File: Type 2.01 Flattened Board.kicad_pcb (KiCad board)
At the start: 4 copper layers, 170 x 170 mm, 74 parts, among them J1 Conn_02x28_Odd_Even, J10 Conn_01x02, J2 Conn_02x18_Odd_Even, J3 Conn_01x01, J4 Conn_02x03_Odd_Even, J5 Conn_02x03_Odd_Even, J6 Conn_02x28_Odd_Even, J7 Conn_01x08, J8 Conn_01x01, J9 Conn_01x01, U1 74LVC1G79, U11 74AHC245, U13 74AHC04, U14 ATmega4809-PF, U16 ATmega4809-PF, U17 74AHC157, U18 74AHC573, U19 74AHC573, U2 74AHC245, U20 Adafruit_FeatherWing, U21 Adafruit_FeatherWing, U3 74AHC138, U4 74AHC245, U5 74AHC245, U6 74AHC245, U7 74LVC8T245, U8 74LVC8T245, U9 i960Sx_PLCC84

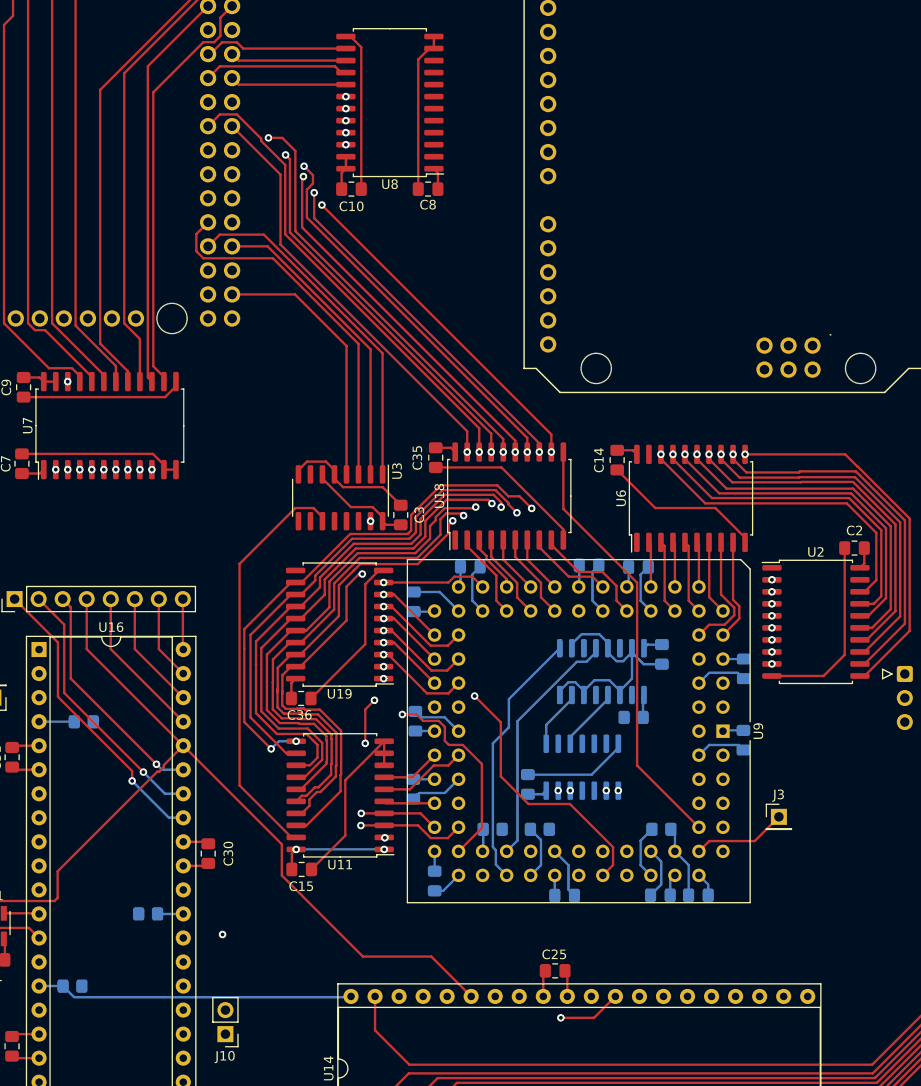
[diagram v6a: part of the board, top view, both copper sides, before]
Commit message: More traces laid out
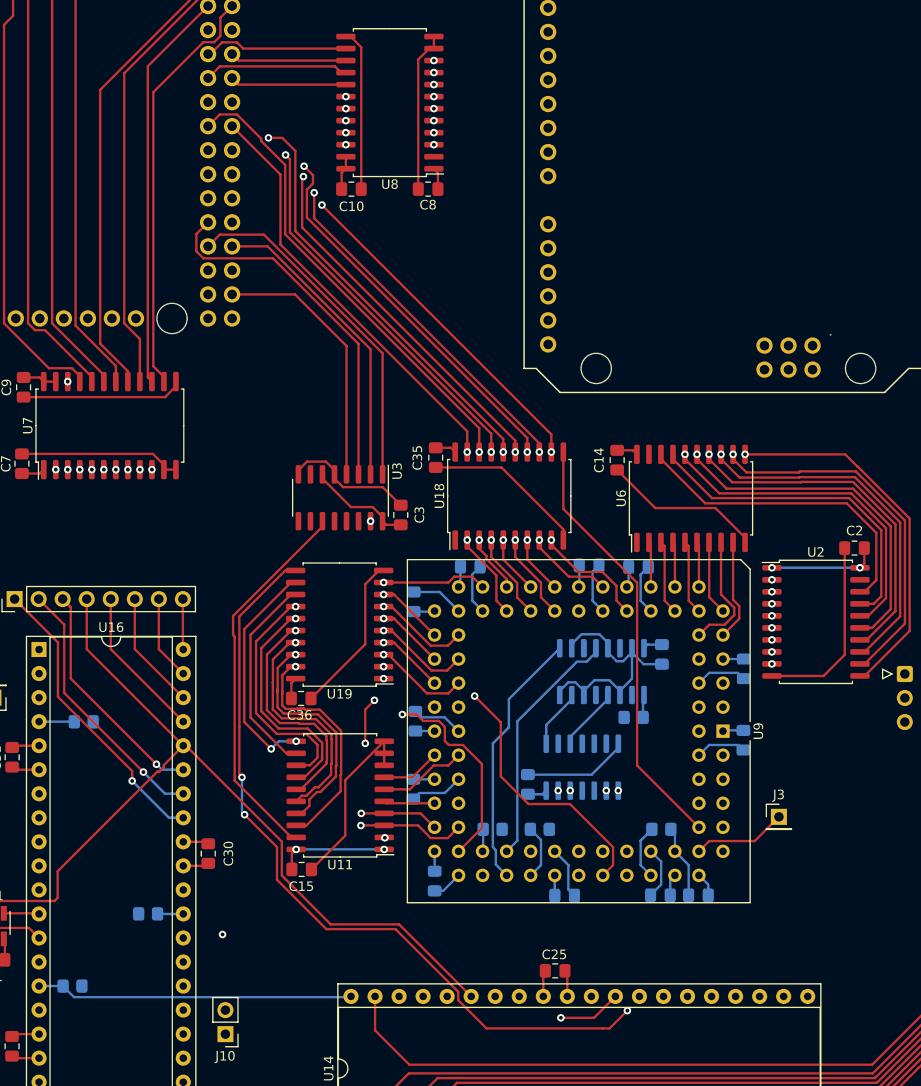
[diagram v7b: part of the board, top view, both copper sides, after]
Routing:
- net /i960/ALE: track 45.6 -> 151.3 mm, vias 0 -> 3
- net /GCM4.L7: track 175.3 -> 112.5 mm, vias 6 -> 5
- net /GCM4.L6: track 169.4 -> 106.7 mm, vias 4 -> 3
- net /i960.D15: track 12.3 -> 69.9 mm, vias 0 -> 2
- net /i960.D14: track 9.21 -> 64.6 mm, vias 0 -> 2
- net /i960.D13: track 6.16 -> 59.7 mm, vias 0 -> 2
- net /i960.D12: track 9.23 -> 60.9 mm, vias 0 -> 2
- net /i960.D11: track 6.16 -> 56.0 mm, vias 0 -> 2
- net /i960.D10: track 9.23 -> 57.3 mm, vias 0 -> 2
- net /i960.D9: track 6.16 -> 52.4 mm, vias 0 -> 2
- net /i960.D8: track 9.23 -> 53.3 mm, vias 0 -> 2
- net /GCM4.L5: track 175.9 -> 153.9 mm
- net /GCM4.L4: track 167.7 -> 149.0 mm
- net /GCM4.L3: track 172.2 -> 154.6 mm
- net /GCM4.L2: track 166.7 -> 149.3 mm
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
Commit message: More wiring
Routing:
- net /GCM4.L6: track 106.7 -> 172.5 mm, vias 3 -> 4
- net /GCM4.L7: track 112.5 -> 176.7 mm, vias 5 -> 6
- net /GCM4.L2: track 149.3 -> 176.0 mm
- net /GCM4.L1: track 152.9 -> 179.6 mm, vias 2 -> 3
- net /GCM4.L5: track 153.9 -> 180.5 mm
- net /GCM4.L0: track 146.9 -> 173.5 mm, vias 2 -> 3
- net /GCM4.L4: track 149.0 -> 174.6 mm
- net /GCM4.L3: track 154.6 -> 179.9 mm
- net /i960/i960.~{INT0}: track 2.35 -> 22.9 mm, vias 0 -> 2
- net /i960/i960.~{INT3}: track 5.78 -> 17.8 mm, vias 0 -> 2
- net /i960.DT\~{R}: track 90.0 -> 91.1 mm
- net /i960.D0: track 51.2 -> 52.1 mm
- net /i960.D1: track 50.3 -> 51.1 mm
- net /i960.D2: track 45.6 -> 46.1 mm
